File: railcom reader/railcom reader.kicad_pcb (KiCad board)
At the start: 2 copper layers, 29 parts, among them J1 DCC_INPUT, J2 Signal output 1, U1 LM339, U2 L7805

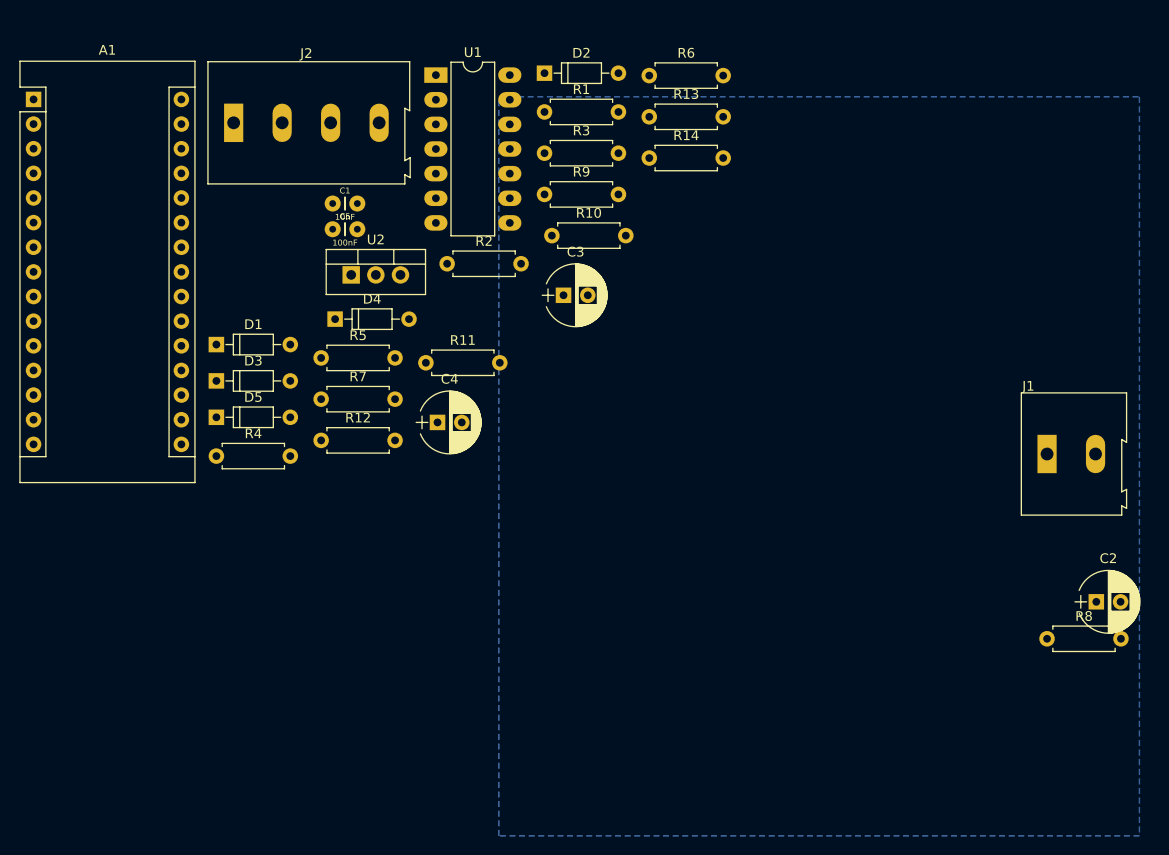
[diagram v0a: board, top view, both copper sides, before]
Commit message: update schematic, netlist, pcb concept
modifications in comparing to railcom specification docs

original "splice" graphic found in topic was a bit confusing (imho)
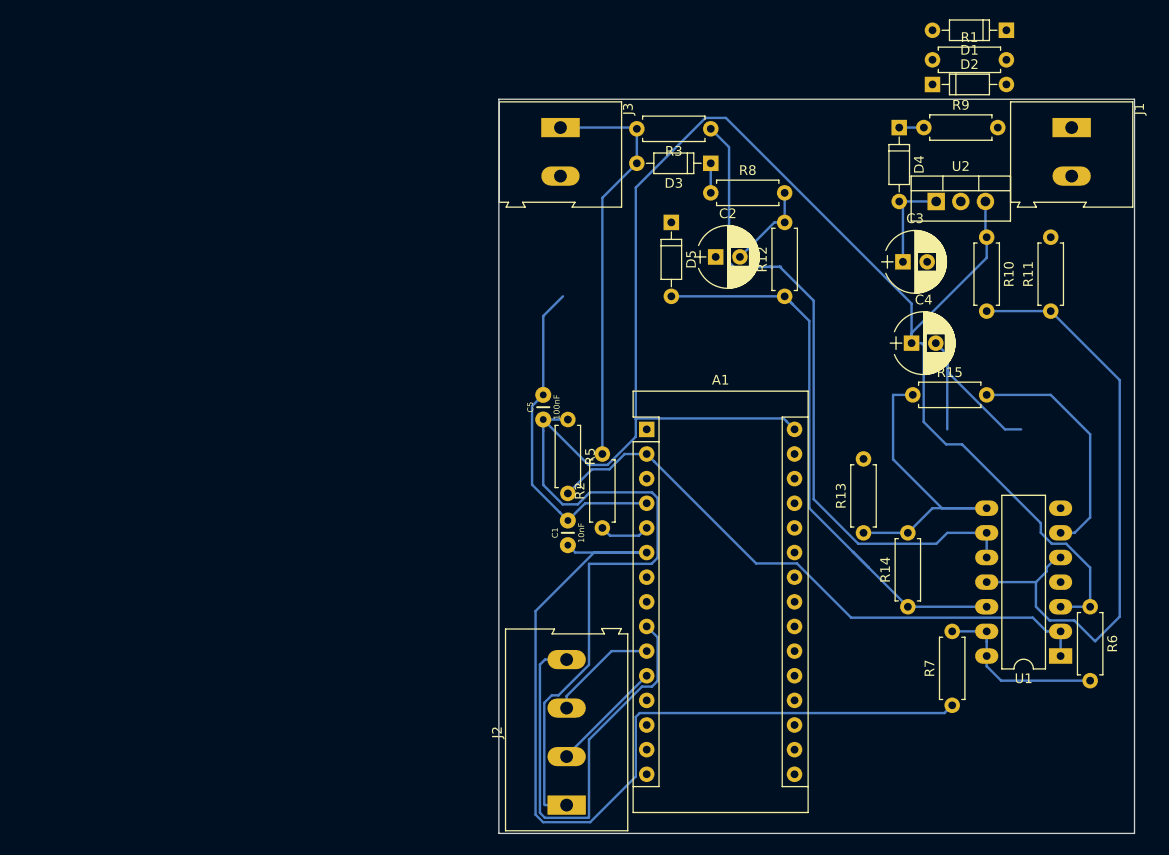
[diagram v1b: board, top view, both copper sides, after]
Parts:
- removed R4: 1K, Resistors_THT:R_Axial_DIN0207_L6.3mm_D2.5mm_P7.62mm_Horizontal
- added J3: TRACK_OUT, Connectors_Terminal_Blocks:TerminalBlock_Altech_AK300-2_P5.00mm, F.Cu at (130.8, 93.3)
- added R15: 0, Resistors_THT:R_Axial_DIN0207_L6.3mm_D2.5mm_P7.62mm_Horizontal, F.Cu at (167.1, 120.9)
- J1: value DCC_INPUT -> BOOSTER_IN
- moved U1 88.0 mm to (182.4, 147.8), turned to 180 degrees
- moved D1 87.7 mm to (176.8, 83.3), turned to 180 degrees
- moved J2 78.3 mm to (131.4, 163.2), turned to 90 degrees
- moved R7 72.3 mm to (171.2, 152.9), turned to 90 degrees
- moved A1 71.8 mm to (139.7, 124.5)
- moved R6 71.2 mm to (185.4, 142.7), turned to 270 degrees
- moved R11 64.6 mm to (181.4, 112.3), turned to 90 degrees
- moved D4 61.4 mm to (165.7, 93.3), turned to 270 degrees
- moved U2 60.8 mm to (169.5, 101.0)
- moved R8 57.6 mm to (146.3, 100.1)
- moved D3 55.7 mm to (146.3, 97.0), turned to 180 degrees
- moved R14 53.4 mm to (166.6, 142.7), turned to 90 degrees
- moved C2 53.0 mm to (146.8, 106.7)
- moved D5 51.0 mm to (142.2, 103.1), turned to 270 degrees
- moved R12 50.0 mm to (153.9, 110.7), turned to 90 degrees
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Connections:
- net /D2 renamed /DCC_IN
- net /D3 renamed /WINDOW_DETECT
- net /RX renamed /RAILCOM_IN
- A1 pad 27: +5V -> Net-(A1-Pad27)
- A1 pad 30: Net-(A1-Pad30) -> /+5V
- C4 pad 1: +5V -> /+5V
- C5 pad 1: +5V -> /+5V
- D1 pad 1: /DECODER -> GND
- D2 pad 2: /DECODER -> GND
- D5 pad 2: Net-(D5-Pad2) -> /VCC
- J1 pad 1: /DCC -> /BOOSTER_IN_A
- J2 pad 1: +5V -> /+5V
- R1 pad 2: /DECODER -> GND
- R10 pad 1: +5V -> /+5V
- R12 pad 1: Net-(D5-Pad2) -> /VCC
- R14 pad 1: Net-(D5-Pad2) -> /VCC
- R5 pad 1: +5V -> /+5V
- R6 pad 1: +5V -> /+5V
- R9 pad 2: /DCC -> /BOOSTER_IN_A
- U1 pad 12: VCC -> /VCC
- U1 pad 3: +5V -> /+5V
- U1 pad 4: /DECODER -> GND
- U1 pad 7: /DECODER -> GND
- U2 pad 3: +5V -> /+5V
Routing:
- net /+5V: track 0.00 -> 222.5 mm
- net /WINDOW_DETECT: track 0.00 -> 95.3 mm
- net Net-(R3-Pad1): track 0.00 -> 68.6 mm
- net /+18mV: track 0.00 -> 63.7 mm
- net /RAILCOM_IN: track 0.00 -> 62.6 mm
- net /VCC: track 0.00 -> 60.5 mm
- net /-18mV: track 0.00 -> 59.2 mm
- net GND: track 0.00 -> 56.0 mm
- net Net-(A1-Pad9): track 0.00 -> 47.2 mm
- net /DCC: track 0.00 -> 42.9 mm
- net Net-(R6-Pad2): track 0.00 -> 18.4 mm
- net Net-(A1-Pad11): track 0.00 -> 11.8 mm
- net Net-(A1-Pad10): track 0.00 -> 11.4 mm
- net Net-(C3-Pad1): track 0.00 -> 10.2 mm
- net Net-(C2-Pad2): track 0.00 -> 9.13 mm
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- removed copper zone on B.Cu, net GND
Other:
- board outline added: 65.5 x 75.7 mm

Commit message: updated net labels & corrected some mistakes.
still getting 10 volts on the 7805. why though?
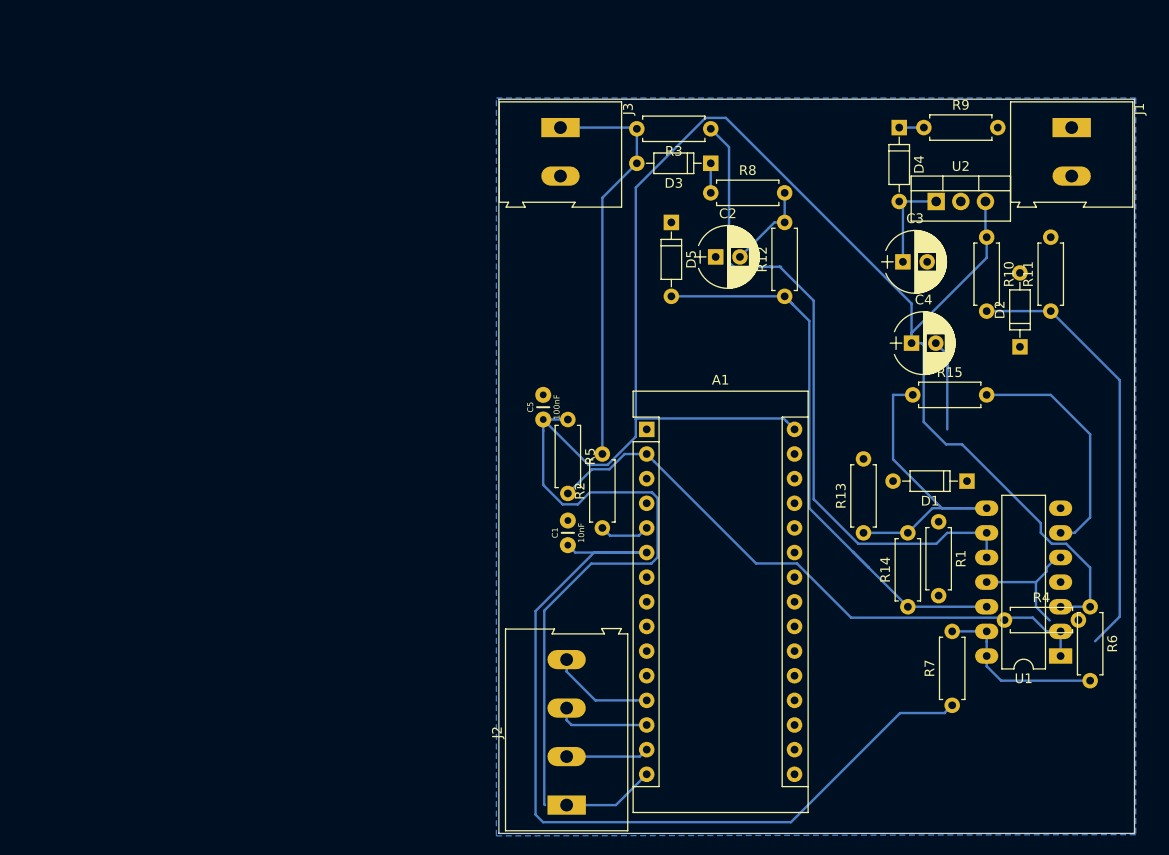
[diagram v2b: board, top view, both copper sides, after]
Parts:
- added R4: 1K, Resistors_THT:R_Axial_DIN0207_L6.3mm_D2.5mm_P7.62mm_Horizontal, F.Cu at (176.6, 144.1)
- moved R1 47.6 mm to (169.8, 134.0), turned to 270 degrees
- moved D1 46.7 mm to (172.7, 129.8)
- moved D2 28.5 mm to (178.2, 116.0), turned to 90 degrees
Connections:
- A1 pad 1: Net-(A1-Pad1) -> (no net)
- A1 pad 10: Net-(A1-Pad10) -> (no net)
- A1 pad 11: Net-(A1-Pad11) -> (no net)
- A1 pad 16: Net-(A1-Pad16) -> (no net)
- A1 pad 17: Net-(A1-Pad17) -> (no net)
- A1 pad 18: Net-(A1-Pad18) -> (no net)
- A1 pad 19: Net-(A1-Pad19) -> (no net)
- A1 pad 20: Net-(A1-Pad20) -> (no net)
- A1 pad 21: Net-(A1-Pad21) -> (no net)
- A1 pad 22: Net-(A1-Pad22) -> (no net)
- A1 pad 23: Net-(A1-Pad23) -> (no net)
- A1 pad 24: Net-(A1-Pad24) -> (no net)
- A1 pad 25: Net-(A1-Pad25) -> (no net)
- A1 pad 26: Net-(A1-Pad26) -> (no net)
- A1 pad 27: Net-(A1-Pad27) -> (no net)
- A1 pad 28: Net-(A1-Pad28) -> (no net)
- A1 pad 3: Net-(A1-Pad3) -> (no net)
- A1 pad 7: Net-(A1-Pad7) -> (no net)
- A1 pad 8: Net-(A1-Pad8) -> (no net)
- A1 pad 9: Net-(A1-Pad9) -> (no net)
- J2 pad 1: /+5V -> Net-(A1-Pad15)
- J2 pad 2: Net-(A1-Pad11) -> Net-(A1-Pad14)
- J2 pad 3: Net-(A1-Pad10) -> Net-(A1-Pad13)
- J2 pad 4: Net-(A1-Pad9) -> Net-(A1-Pad12)
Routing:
- net Net-(A1-Pad9): track 47.2 -> 0.00 mm
- net GND: track 56.0 -> 11.0 mm
- net Net-(A1-Pad11): track 11.8 -> 0.00 mm
- net Net-(A1-Pad10): track 11.4 -> 0.00 mm
- net Net-(A1-Pad12): track 0.00 -> 10.7 mm
- net Net-(A1-Pad13): track 0.00 -> 9.70 mm
- net Net-(A1-Pad15): track 0.00 -> 9.57 mm
- net Net-(A1-Pad14): track 0.00 -> 8.63 mm
- net /+18mV: track 63.7 -> 58.1 mm
- net /WINDOW_DETECT: track 95.3 -> 91.7 mm
- net /+5V: track 222.5 -> 219.7 mm
- added copper zone on B.Cu, net GND
